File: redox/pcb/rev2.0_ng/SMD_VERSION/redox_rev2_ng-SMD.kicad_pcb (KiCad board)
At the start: 2 copper layers, 162.2 x 138.8 mm, 153 parts, among them J2 OLED-SSD1306, K1 KEYSW, K10 KEYSW, K11 KEYSW, K12 KEYSW, K13 KEYSW, K14 KEYSW, K15 KEYSW, K16 KEYSW, K17 KEYSW, K18 KEYSW, K19 KEYSW, K2 KEYSW, K20 KEYSW, K21 KEYSW, K22 KEYSW, K23 KEYSW, K24 KEYSW, K25 KEYSW, K26 KEYSW, K27 KEYSW, K28 KEYSW, K29 KEYSW, K3 KEYSW, K30 KEYSW, K31 KEYSW, K32 KEYSW, K33 KEYSW, K34 KEYSW, K35 KEYSW, K4 KEYSW, K5 KEYSW, K6 KEYSW, K7 KEYSW, K8 KEYSW, K9 KEYSW, P1 TC2030-AVR, Q1 2N7002, U1 PRTR5V0U2X, U2 ATmega32U4, Y1 16Mhz

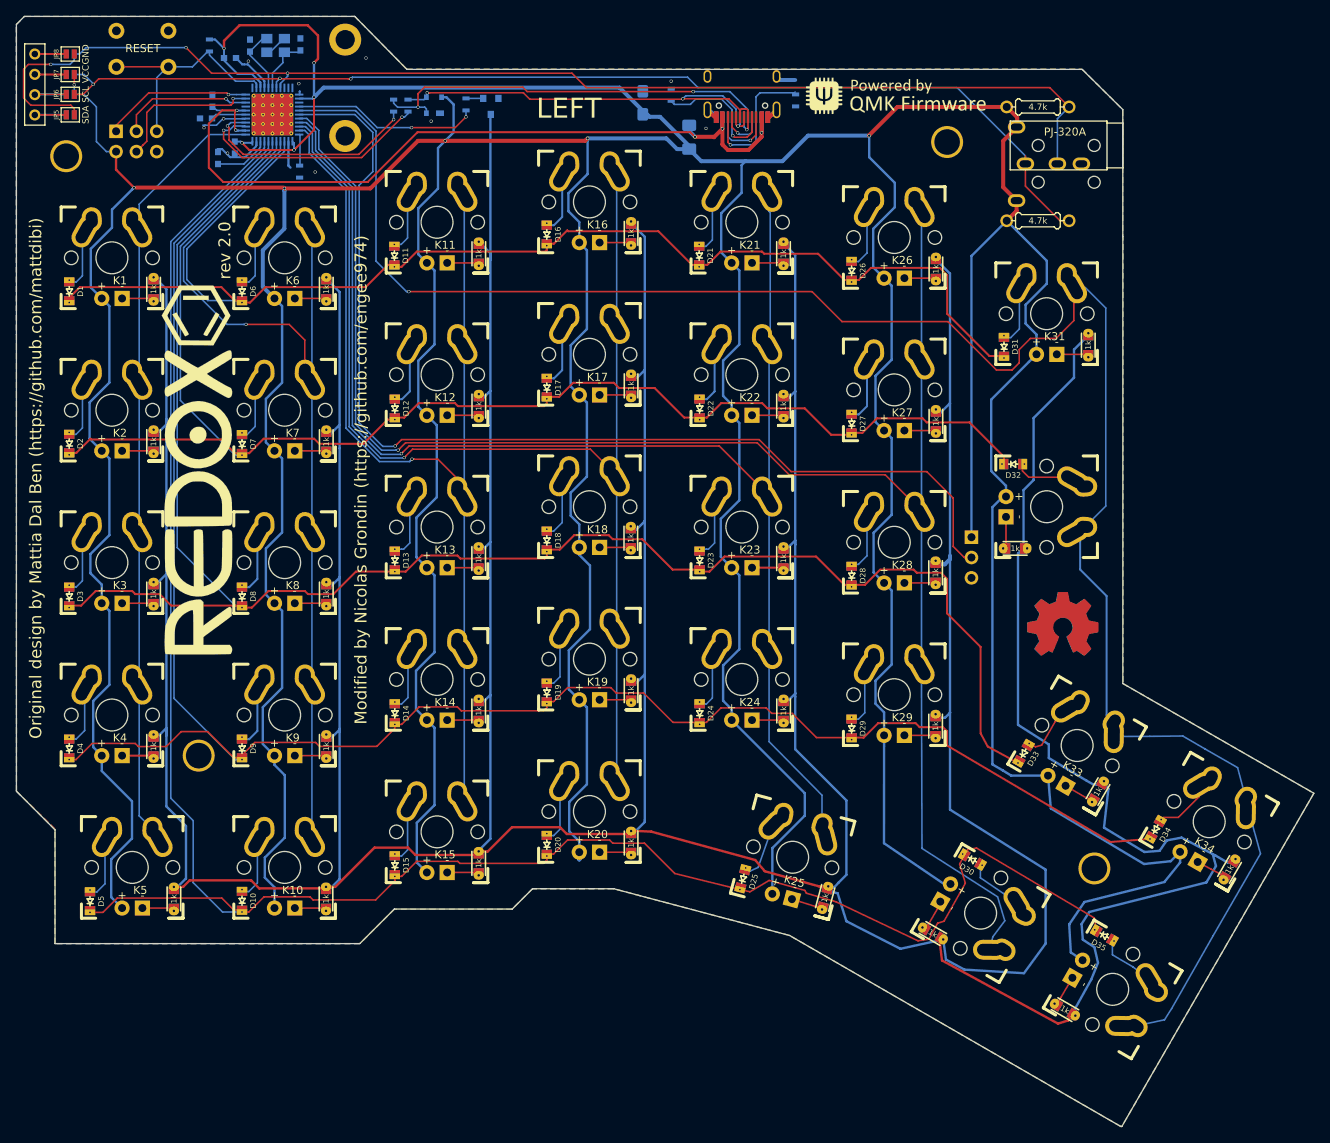
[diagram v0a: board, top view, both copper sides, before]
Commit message: Change PCB holes placement, TRSS connector, add JLC id.
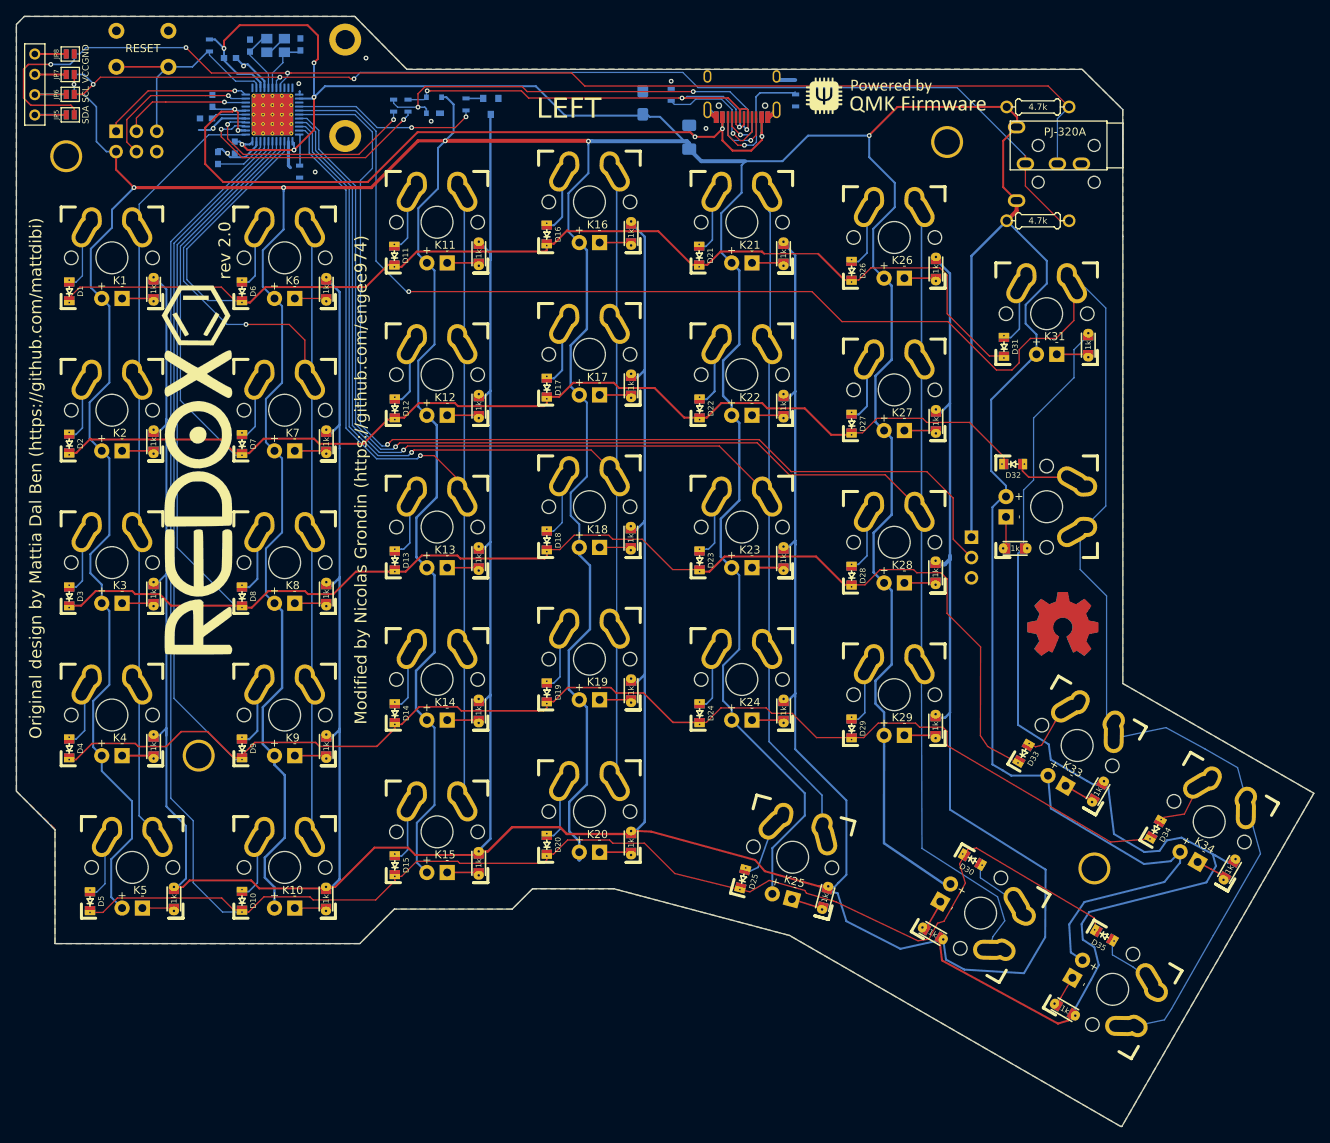
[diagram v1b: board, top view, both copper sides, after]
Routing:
- net MOSI: track 18.8 -> 20.7 mm
- net LEDGND: track 817.9 -> 817.1 mm
- net SCL: track 140.1 -> 140.9 mm
- net GND: track 33.0 -> 33.7 mm, vias 10 -> 9
- net rgb_data: track 134.9 -> 134.2 mm
- net D-: track 30.6 -> 31.2 mm
- net VBUS: track 102.8 -> 103.4 mm
- net SCK: track 16.7 -> 16.1 mm
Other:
- net class Default: clearance 0.2 -> 0.15; trace_width 0.2 -> 0.15; via_dia 0.4 -> 0.6
- net class GND: clearance 0.2 -> 0.15; trace_width 0.5 -> 0.4; via_dia 0.4 -> 0.6
- net class VBUS: clearance 0.2 -> 0.15; trace_width 0.5 -> 0.25; via_dia 0.4 -> 0.6
- net class VCC: clearance 0.2 -> 0.15; trace_width 0.3 -> 0.25; via_dia 0.4 -> 0.6
- rule trace_clearance: 0.2 -> 0.15
- rule trace_min: 0.2 -> 0.15
- rule via_min_size: 0.4 -> 0.6
